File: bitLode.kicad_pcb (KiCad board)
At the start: 4 copper layers, 13.2 x 30 mm, 30 parts, among them J1 USB_C_Receptacle_USB2.0, J2 Conn_02x07_Odd_Even, U2 W25Q16JVUXIQ, U3 RP2040, U4 AP2112K-3.3TRG1, Y1 12MHz

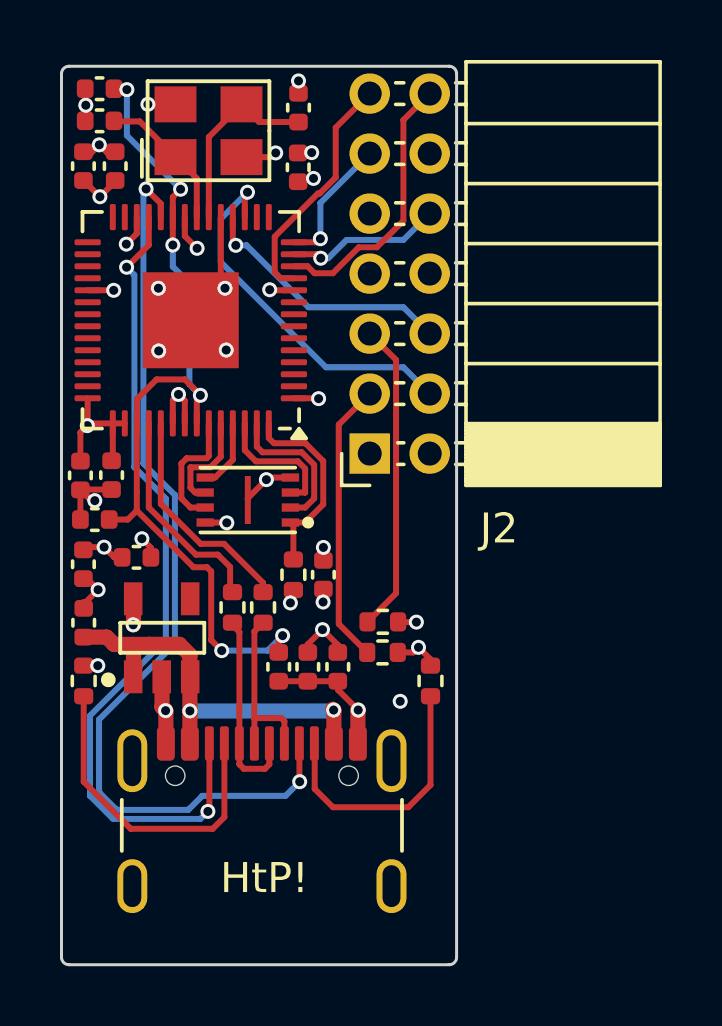
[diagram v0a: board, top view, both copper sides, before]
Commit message: Fixed the Orientation
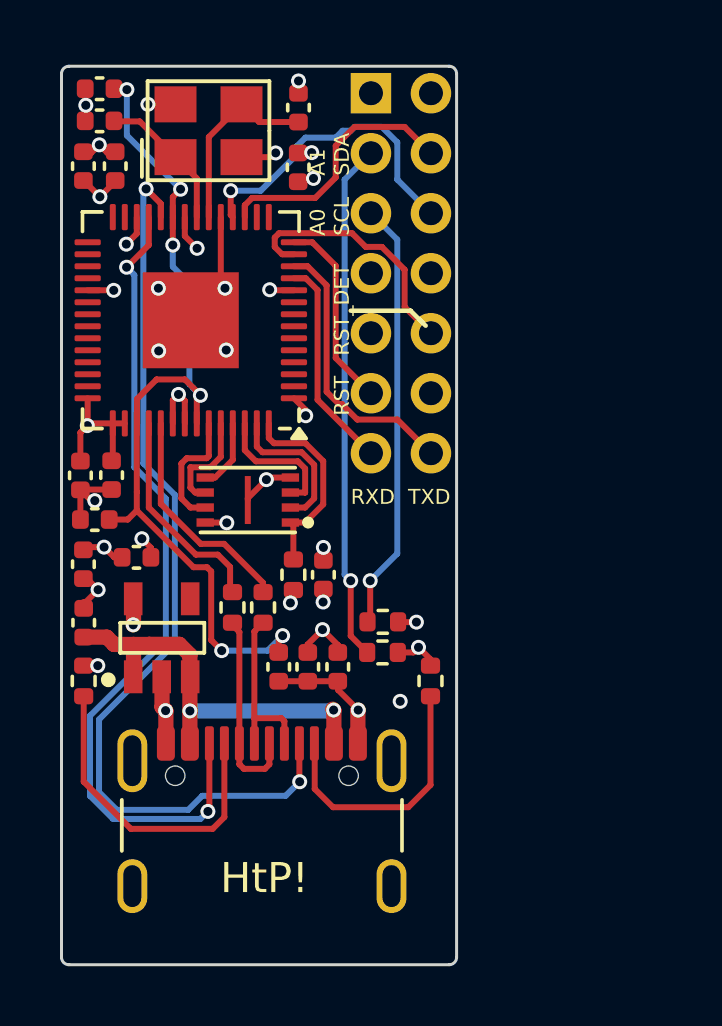
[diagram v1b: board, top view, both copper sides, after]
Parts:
- J2: moved to B.Cu
- moved J2 12.0 mm to (124.7, 81.8)
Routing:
- net /A1: track 9.97 -> 17.3 mm, vias 0 -> 1
- net /A0: track 10.4 -> 14.9 mm, vias 0 -> 1
- net /SDA: track 12.4 -> 8.67 mm, vias 1 -> 0
- net /RST_DET: track 5.20 -> 8.43 mm, vias 1 -> 0
- net /RST: track 4.45 -> 6.97 mm, vias 1 -> 0
- net /SCL: track 8.66 -> 10.5 mm
- net /TXD: track 8.02 -> 7.13 mm
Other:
- board text added: "A0 SCL"
- board text added: "A1 SDA"
- board text added: "RST"
- board text added: "RST_DET"
- board text added: "RXD TXD"
